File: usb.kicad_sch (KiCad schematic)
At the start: 24 parts, among them J201 USB_C_Receptacle_USB2.0_16P, J202 Screw_Terminal_01x02, Q1 STL6N3LLH6, U5 TCPP01-M12, U6 USBLC6-2P6, U7 STEF05SGR

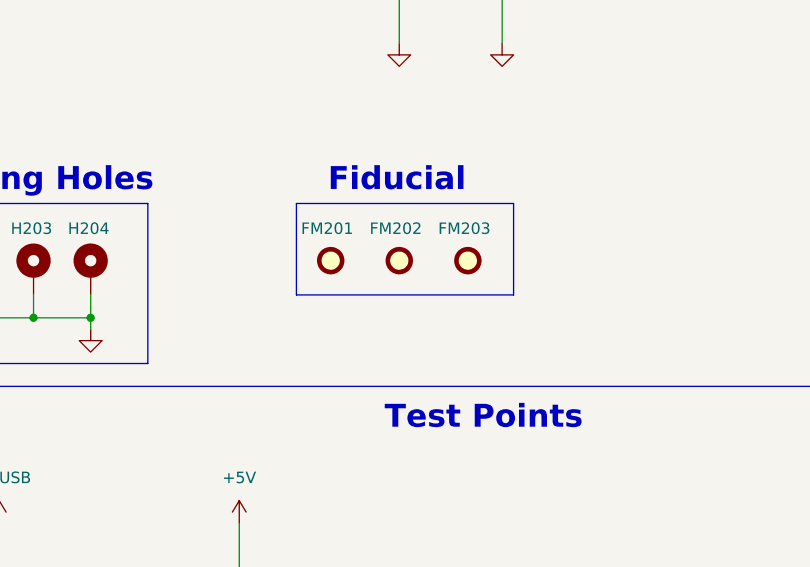
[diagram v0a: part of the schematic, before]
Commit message: fine tune high speed traces
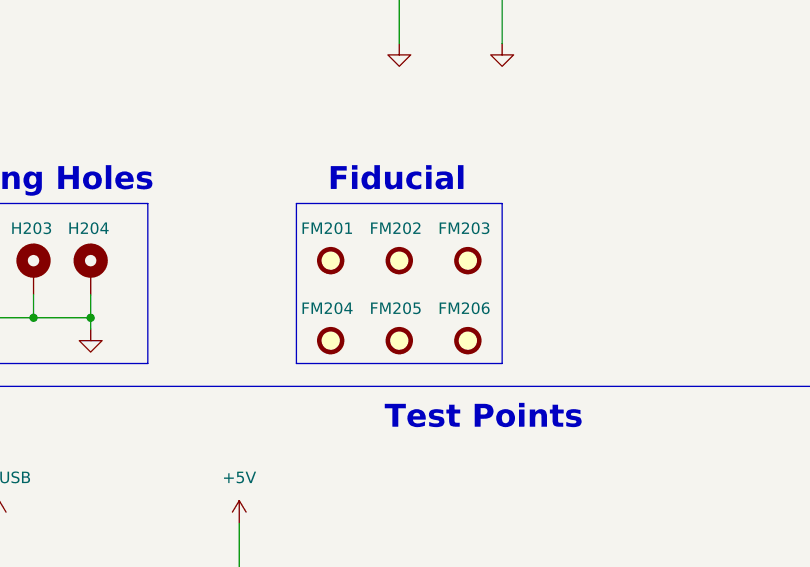
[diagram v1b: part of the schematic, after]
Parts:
- added FM204, FM205, FM206: Fiducial, Fiducial:Fiducial_1mm_Mask2mm, symbol Mechanical:Fiducial
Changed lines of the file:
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@@
 	(rectangle
 		(start 64.77 147.32)
-		(end 88.9 157.48)
+		(end 87.63 165.1)
 		(stroke
 			(width 0)
@@
 	)
 	(symbol
+		(lib_id "Mechanical:Fiducial")
+		(at 83.82 162.56 0)
+		(unit 1)
+		(exclude_from_sim yes)
+		(in_bom no)
+		(on_board yes)
+		(dnp no)
+		(property "Reference" "FM206"
+			(at 80.518 159.004 0)
+			(effects
+				(font
+					(size 1.27 1.27)
+				)
+				(justify left)
+			)
+		)
+		(property "Value" "Fiducial"
+			(at 86.36 163.8299 0)
+			(effects
+				(font
+					(size 1.27 1.27)
+				)
+				(justify left)
+				(hide yes)
+			)
+		)
+		(property "Footprint" "Fiducial:Fiducial_1mm_Mask2mm"
+			(at 83.82 162.56 0)
+			(effects
+				(font
+					(size 1.27 1.27)
+				)
+				(hide yes)
+			)
+		)
+		(property "Datasheet" "~"
+			(at 83.82 162.56 0)
+			(effects
+				(font
+					(size 1.27 1.27)
+				)
+				(hide yes)
+			)
+		)
+		(property "Description" "Fiducial Marker"
+			(at 83.82 162.56 0)
+			(effects
+				(font
+					(size 1.27 1.27)
+				)
+				(hide yes)
+			)
+		)
+		(instances
+			(project "EnergyMonitoringSystem"
+				(path "/e660428c-c9b7-476c-8ac8-2d419f233469/7dd15615-8075-471d-b8bf-599b8660331d"
+					(reference "FM206")
+					(unit 1)
+				)
+			)
+		)
+	)
+	(symbol
 		(lib_id "EMS:+V_USB")
 		(at 31.75 182.88 0)
@@
 	)
 	(symbol
+		(lib_id "Mechanical:Fiducial")
+		(at 76.2 162.56 0)
+		(unit 1)
+		(exclude_from_sim yes)
+		(in_bom no)
+		(on_board yes)
+		(dnp no)
+		(property "Reference" "FM205"
+			(at 72.898 159.004 0)
+			(effects
+				(font
+					(size 1.27 1.27)
+				)
+				(justify left)
+			)
+		)
+		(property "Value" "Fiducial"
+			(at 78.74 163.8299 0)
+			(effects
+				(font
+					(size 1.27 1.27)
+				)
+				(justify left)
+				(hide yes)
+			)
+		)
+		(property "Footprint" "Fiducial:Fiducial_1mm_Mask2mm"
+			(at 76.2 162.56 0)
+			(effects
+				(font
+					(size 1.27 1.27)
+				)
+				(hide yes)
+			)
+		)
+		(property "Datasheet" "~"
+			(at 76.2 162.56 0)
+			(effects
+				(font
+					(size 1.27 1.27)
+				)
+				(hide yes)
+			)
+		)
+		(property "Description" "Fiducial Marker"
+			(at 76.2 162.56 0)
+			(effects
+				(font
+					(size 1.27 1.27)
+				)
+				(hide yes)
+			)
+		)
+		(instances
+			(project "EnergyMonitoringSystem"
+				(path "/e660428c-c9b7-476c-8ac8-2d419f233469/7dd15615-8075-471d-b8bf-599b8660331d"
+					(reference "FM205")
+					(unit 1)
+				)
+			)
+		)
+	)
+	(symbol
 		(lib_id "power:PWR_FLAG")
 		(at 190.5 101.6 90)
@@
 					(unit 1)
 				)
+			)
+		)
+	)
+	(symbol
+		(lib_id "Mechanical:Fiducial")
+		(at 68.58 162.56 0)
+		(unit 1)
+		(exclude_from_sim yes)
+		(in_bom no)
+		(on_board yes)
+		(dnp no)
+		(property "Reference" "FM204"
+			(at 65.278 159.004 0)
+			(effects
+				(font
+					(size 1.27 1.27)
+				)
+				(justify left)
+			)
+		)
+		(property "Value" "Fiducial"
+			(at 71.12 163.8299 0)
+			(effects
+				(font
+					(size 1.27 1.27)
+				)
+				(justify left)
+				(hide yes)
+			)
+		)
+		(property "Footprint" "Fiducial:Fiducial_1mm_Mask2mm"
+			(at 68.58 162.56 0)
+			(effects
+				(font
+					(size 1.27 1.27)
+				)
+				(hide yes)
+			)
+		)
+		(property "Datasheet" "~"
+			(at 68.58 162.56 0)
+			(effects
+				(font
+					(size 1.27 1.27)
+				)
+				(hide yes)
+			)
+		)
+		(property "Description" "Fiducial Marker"
+			(at 68.58 162.56 0)
+			(effects
+				(font
+					(size 1.27 1.27)
+				)
+				(hide yes)
+			)
+		)
+		(instances
+			(project "EnergyMonitoringSystem"
+				(path "/e660428c-c9b7-476c-8ac8-2d419f233469/7dd15615-8075-471d-b8bf-599b8660331d"
+					(reference "FM204")
+					(unit 1)
+				)
